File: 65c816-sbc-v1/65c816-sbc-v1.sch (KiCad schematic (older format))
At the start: 50 parts, among them J1 EXPANSION, J2 SIO, J3 VIA_A, J4 VIA_B, J5 power, SW1 RESET, SW2 NMI, U1 W65C816SxP, U10 W65C22SxP, U11 W65C51NxP, U12 74HC138, U15 74HC74, U2 74HC573, U3 74HC245, U4 PAL20L8, U5 PAL20L8, U6 74HC244, U7 74HC244, U8 AS6C4008-55PCN, U9 28C256, X1 28MHz, Y1 1.8432MHz

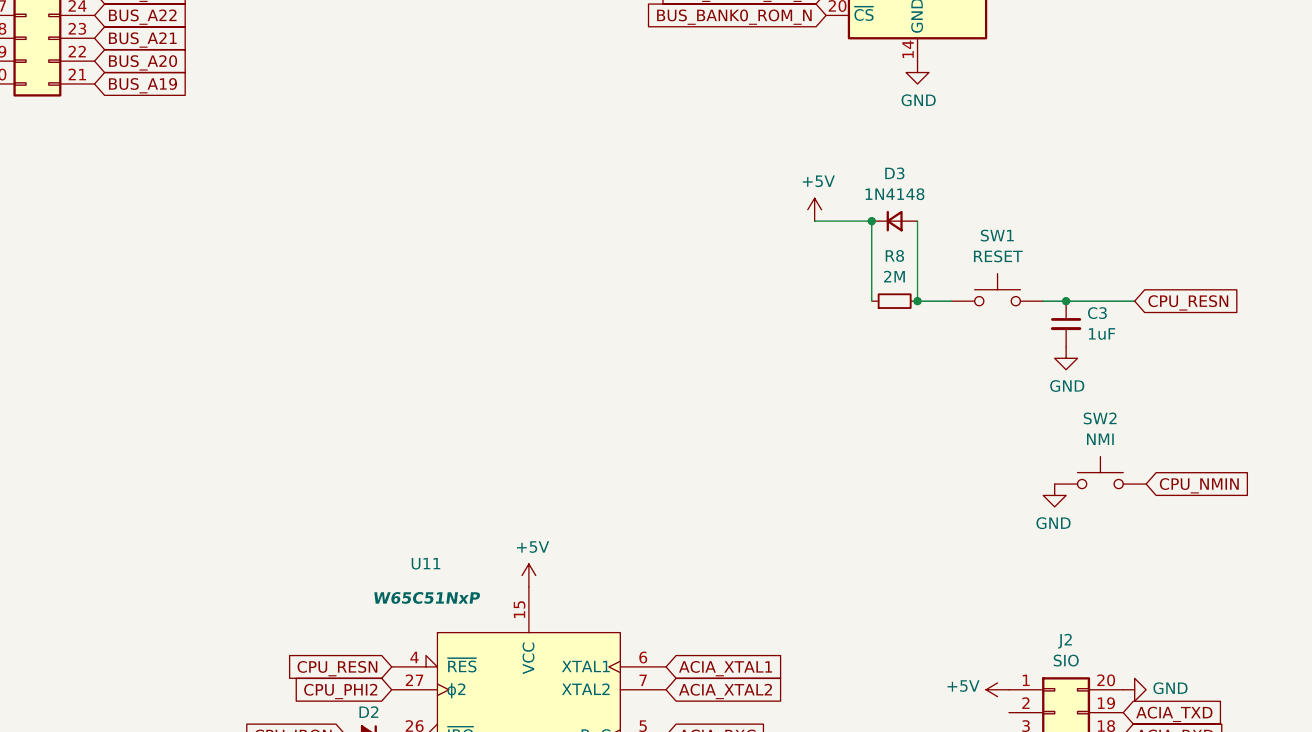
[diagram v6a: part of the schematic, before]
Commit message: Add some LEDs, I may want to wire them up to make sure I'm doing the right thing? Dunno yet.
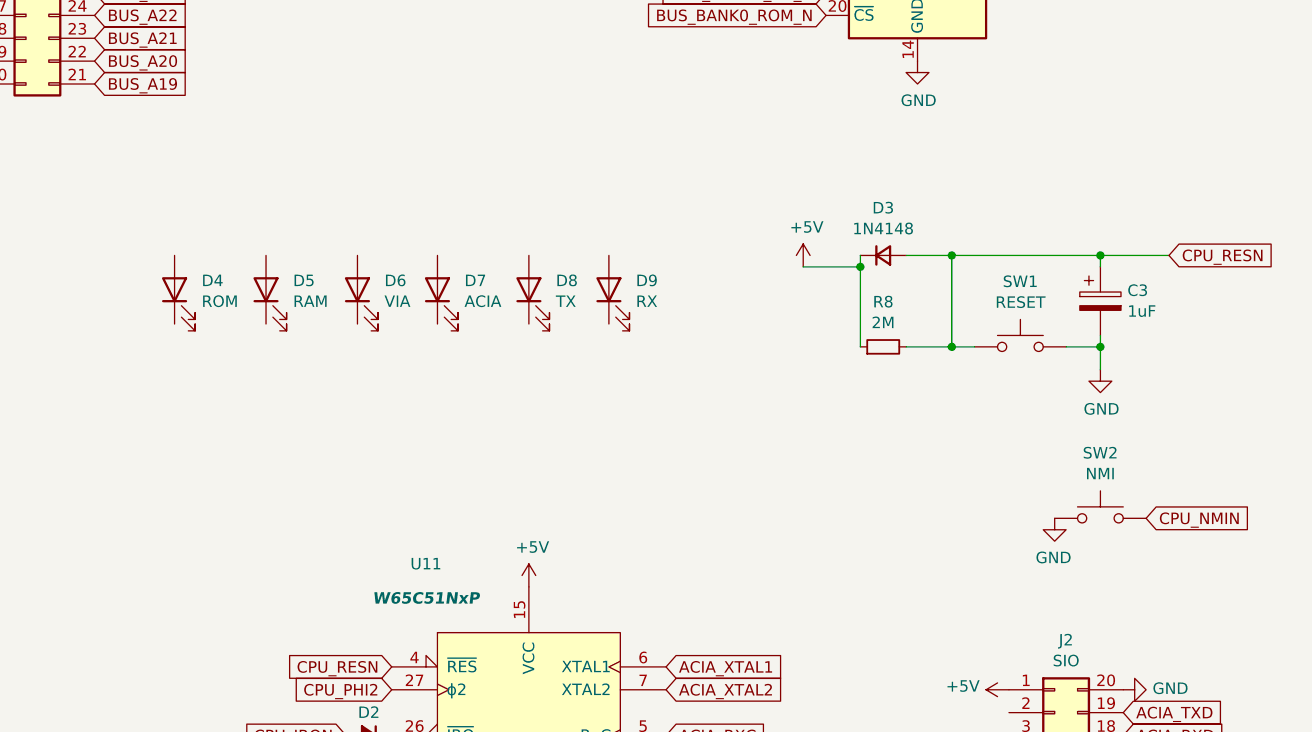
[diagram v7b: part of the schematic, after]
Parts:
- removed C3: 1uF, symbol Device:C_Small
- added C3: 1uF, symbol Device:CP
- added D4: ROM, symbol Device:LED
- added D5: RAM, symbol Device:LED
- added D6: VIA, symbol Device:LED
- added D7: ACIA, symbol Device:LED
- added D8: TX, symbol Device:LED
- added D9: RX, symbol Device:LED
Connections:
- net CPU_RESN: now also D3.2 (A), R8.2, SW1.1, C3.1; no longer SW1.2
- net GND: now also SW1.2, C3.2
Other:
- moved on the sheet: D3, R8, SW1, SW2
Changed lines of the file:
@@
 L Device:D_Small D3
 U 1 1 61DCFAE9
-P 14250 3600
-F 0 "D3" H 14250 3807 50  0000 C CNN
-F 1 "1N4148" H 14250 3716 50  0000 C CNN
-F 2 "Diode_THT:D_DO-35_SOD27_P7.62mm_Horizontal" V 14250 3600 50  0001 C CNN
-F 3 "~" V 14250 3600 50  0001 C CNN
-	1    14250 3600
+P 14200 3750
+F 0 "D3" H 14200 3957 50  0000 C CNN
+F 1 "1N4148" H 14200 3866 50  0000 C CNN
+F 2 "Diode_THT:D_DO-35_SOD27_P7.62mm_Horizontal" V 14200 3750 50  0001 C CNN
+F 3 "~" V 14200 3750 50  0001 C CNN
+	1    14200 3750
 	1    0    0    -1
 $EndComp
@@
 L Device:R_Small R8
 U 1 1 61DD0317
-P 14250 3950
-F 0 "R8" V 14446 3950 50  0000 C CNN
-F 1 "2M" V 14355 3950 50  0000 C CNN
-F 2 "" H 14250 3950 50  0001 C CNN
-F 3 "~" H 14250 3950 50  0001 C CNN
-	1    14250 3950
+P 14200 4150
+F 0 "R8" V 14396 4150 50  0000 C CNN
+F 1 "2M" V 14305 4150 50  0000 C CNN
+F 2 "" H 14200 4150 50  0001 C CNN
+F 3 "~" H 14200 4150 50  0001 C CNN
+	1    14200 4150
 	0    -1   -1   0
-$EndComp
-$Comp
-L Device:C_Small C3
-U 1 1 61DD0F01
-P 15000 4050
-F 0 "C3" H 15092 4096 50  0000 L CNN
-F 1 "1uF" H 15092 4005 50  0000 L CNN
-F 2 "" H 15000 4050 50  0001 C CNN
-F 3 "~" H 15000 4050 50  0001 C CNN
-	1    15000 4050
-	1    0    0    -1
 $EndComp
 $Comp
 L Switch:SW_Push SW1
 U 1 1 61DD2E7B
-P 14700 3950
-F 0 "SW1" H 14700 4235 50  0000 C CNN
-F 1 "RESET" H 14700 4144 50  0000 C CNN
-F 2 "" H 14700 4150 50  0001 C CNN
-F 3 "~" H 14700 4150 50  0001 C CNN
-	1    14700 3950
+P 14800 4150
+F 0 "SW1" H 14800 4435 50  0000 C CNN
+F 1 "RESET" H 14800 4344 50  0000 C CNN
+F 2 "" H 14800 4350 50  0001 C CNN
+F 3 "~" H 14800 4350 50  0001 C CNN
+	1    14800 4150
 	1    0    0    -1
 $EndComp
@@
 L Switch:SW_Push SW2
 U 1 1 61DD3596
-P 15150 4750
-F 0 "SW2" H 15150 5035 50  0000 C CNN
-F 1 "NMI" H 15150 4944 50  0000 C CNN
-F 2 "" H 15150 4950 50  0001 C CNN
-F 3 "~" H 15150 4950 50  0001 C CNN
-	1    15150 4750
+P 15150 4900
+F 0 "SW2" H 15150 5185 50  0000 C CNN
+F 1 "NMI" H 15150 5094 50  0000 C CNN
+F 2 "" H 15150 5100 50  0001 C CNN
+F 3 "~" H 15150 5100 50  0001 C CNN
+	1    15150 4900
 	-1   0    0    -1
 $EndComp
@@
 L power:GND #PWR0141
 U 1 1 61D6FDD3
-P 14950 4750
-F 0 "#PWR0141" H 14950 4500 50  0001 C CNN
-F 1 "GND" H 14955 4577 50  0000 C CNN
-F 2 "" H 14950 4750 50  0001 C CNN
-F 3 "" H 14950 4750 50  0001 C CNN
-	1    14950 4750
+P 14950 4900
+F 0 "#PWR0141" H 14950 4650 50  0001 C CNN
+F 1 "GND" H 14955 4727 50  0000 C CNN
+F 2 "" H 14950 4900 50  0001 C CNN
+F 3 "" H 14950 4900 50  0001 C CNN
+	1    14950 4900
 	-1   0    0    -1
 $EndComp
-Text GLabel 15350 4750 2    50   Input ~ 0
+Text GLabel 15350 4900 2    50   Input ~ 0
 CPU_NMIN
 Wire Wire Line
-	14150 3600 14150 3950
-Wire Wire Line
-	14350 3600 14350 3950
+	14100 3800 14100 4150
 $Comp
 L power:+5V #PWR0142
 U 1 1 61D85F0E
-P 13900 3600
-F 0 "#PWR0142" H 13900 3450 50  0001 C CNN
-F 1 "+5V" H 13915 3773 50  0000 C CNN
-F 2 "" H 13900 3600 50  0001 C CNN
-F 3 "" H 13900 3600 50  0001 C CNN
-	1    13900 3600
-	1    0    0    -1
-$EndComp
-Wire Wire Line
-	13900 3600 14150 3600
-Connection ~ 14150 3600
-Wire Wire Line
-	15000 3950 14900 3950
-Wire Wire Line
-	14500 3950 14350 3950
-Connection ~ 14350 3950
+P 13850 3800
+F 0 "#PWR0142" H 13850 3650 50  0001 C CNN
+F 1 "+5V" H 13865 3973 50  0000 C CNN
+F 2 "" H 13850 3800 50  0001 C CNN
+F 3 "" H 13850 3800 50  0001 C CNN
+	1    13850 3800
+	1    0    0    -1
+$EndComp
+Wire Wire Line
+	13850 3800 14100 3800
 $Comp
 L power:GND #PWR0143
 U 1 1 61D967F7
-P 15000 4150
-F 0 "#PWR0143" H 15000 3900 50  0001 C CNN
-F 1 "GND" H 15005 3977 50  0000 C CNN
-F 2 "" H 15000 4150 50  0001 C CNN
-F 3 "" H 15000 4150 50  0001 C CNN
-	1    15000 4150
-	1    0    0    -1
-$EndComp
-Text GLabel 15300 3950 2    50   Input ~ 0
+P 15150 4250
+F 0 "#PWR0143" H 15150 4000 50  0001 C CNN
+F 1 "GND" H 15155 4077 50  0000 C CNN
+F 2 "" H 15150 4250 50  0001 C CNN
+F 3 "" H 15150 4250 50  0001 C CNN
+	1    15150 4250
+	1    0    0    -1
+$EndComp
+Text GLabel 15450 3750 2    50   Input ~ 0
 CPU_RESN
-Wire Wire Line
-	15300 3950 15000 3950
-Connection ~ 15000 3950
 $Comp
 L Device:C_Small C32
@@
 	1    0    0    -1
 $EndComp
+Wire Wire Line
+	14300 4150 14500 4150
+Wire Wire Line
+	14100 3750 14100 3800
+Connection ~ 14100 3800
+Wire Wire Line
+	14300 3750 14500 3750
+Wire Wire Line
+	14500 3750 14500 4150
+Connection ~ 14500 3750
+Connection ~ 14500 4150
+Wire Wire Line
+	14600 4150 14500 4150
+Wire Wire Line
+	15000 4150 15150 4150
+Wire Wire Line
+	15150 4150 15150 4250
+$Comp
+L Device:CP C3
+U 1 1 61ECEEFB
+P 15150 3950
+F 0 "C3" H 15268 3996 50  0000 L CNN
+F 1 "1uF" H 15268 3905 50  0000 L CNN
+F 2 "" H 15188 3800 50  0001 C CNN
+F 3 "~" H 15150 3950 50  0001 C CNN
+	1    15150 3950
+	1    0    0    -1
+$EndComp
+Wire Wire Line
+	14500 3750 15150 3750
+Wire Wire Line
+	15150 3800 15150 3750
+Connection ~ 15150 3750
+Wire Wire Line
+	15150 3750 15450 3750
+Wire Wire Line
+	15150 4100 15150 4150
+Connection ~ 15150 4150
+$Comp
+L Device:LED D4
+U 1 1 61EE19AC
+P 11100 3900
+F 0 "D4" V 11139 3782 50  0000 R CNN
+F 1 "ROM" V 11048 3782 50  0000 R CNN
+F 2 "" H 11100 3900 50  0001 C CNN
+F 3 "~" H 11100 3900 50  0001 C CNN
+	1    11100 3900
+	0    -1   -1   0
+$EndComp
+$Comp
+L Device:LED D5
+U 1 1 61EEF02B
+P 11500 3900
+F 0 "D5" V 11539 3782 50  0000 R CNN
+F 1 "RAM" V 11448 3782 50  0000 R CNN
+F 2 "" H 11500 3900 50  0001 C CNN
+F 3 "~" H 11500 3900 50  0001 C CNN
+	1    11500 3900
+	0    -1   -1   0
+$EndComp
+$Comp
+L Device:LED D6
+U 1 1 61EF1D84
+P 11900 3900
+F 0 "D6" V 11939 3782 50  0000 R CNN
+F 1 "VIA" V 11848 3782 50  0000 R CNN
+F 2 "" H 11900 3900 50  0001 C CNN
+F 3 "~" H 11900 3900 50  0001 C CNN
+	1    11900 3900
+	0    -1   -1   0
+$EndComp
+$Comp
+L Device:LED D7
+U 1 1 61EF8861
+P 12250 3900
+F 0 "D7" V 12289 3782 50  0000 R CNN
+F 1 "ACIA" V 12198 3782 50  0000 R CNN
+F 2 "" H 12250 3900 50  0001 C CNN
+F 3 "~" H 12250 3900 50  0001 C CNN
+	1    12250 3900
+	0    -1   -1   0
+$EndComp
+$Comp
+L Device:LED D8
+U 1 1 61EFD25B
+P 12650 3900
+F 0 "D8" V 12689 3782 50  0000 R CNN
+F 1 "TX" V 12598 3782 50  0000 R CNN
+F 2 "" H 12650 3900 50  0001 C CNN
+F 3 "~" H 12650 3900 50  0001 C CNN
+	1    12650 3900
+	0    -1   -1   0
+$EndComp
+$Comp
+L Device:LED D9
+U 1 1 61F004E4
+P 13000 3900
+F 0 "D9" V 13039 3782 50  0000 R CNN
+F 1 "RX" V 12948 3782 50  0000 R CNN
+F 2 "" H 13000 3900 50  0001 C CNN
+F 3 "~" H 13000 3900 50  0001 C CNN
+	1    13000 3900
+	0    -1   -1   0
+$EndComp
 $EndSCHEMATC

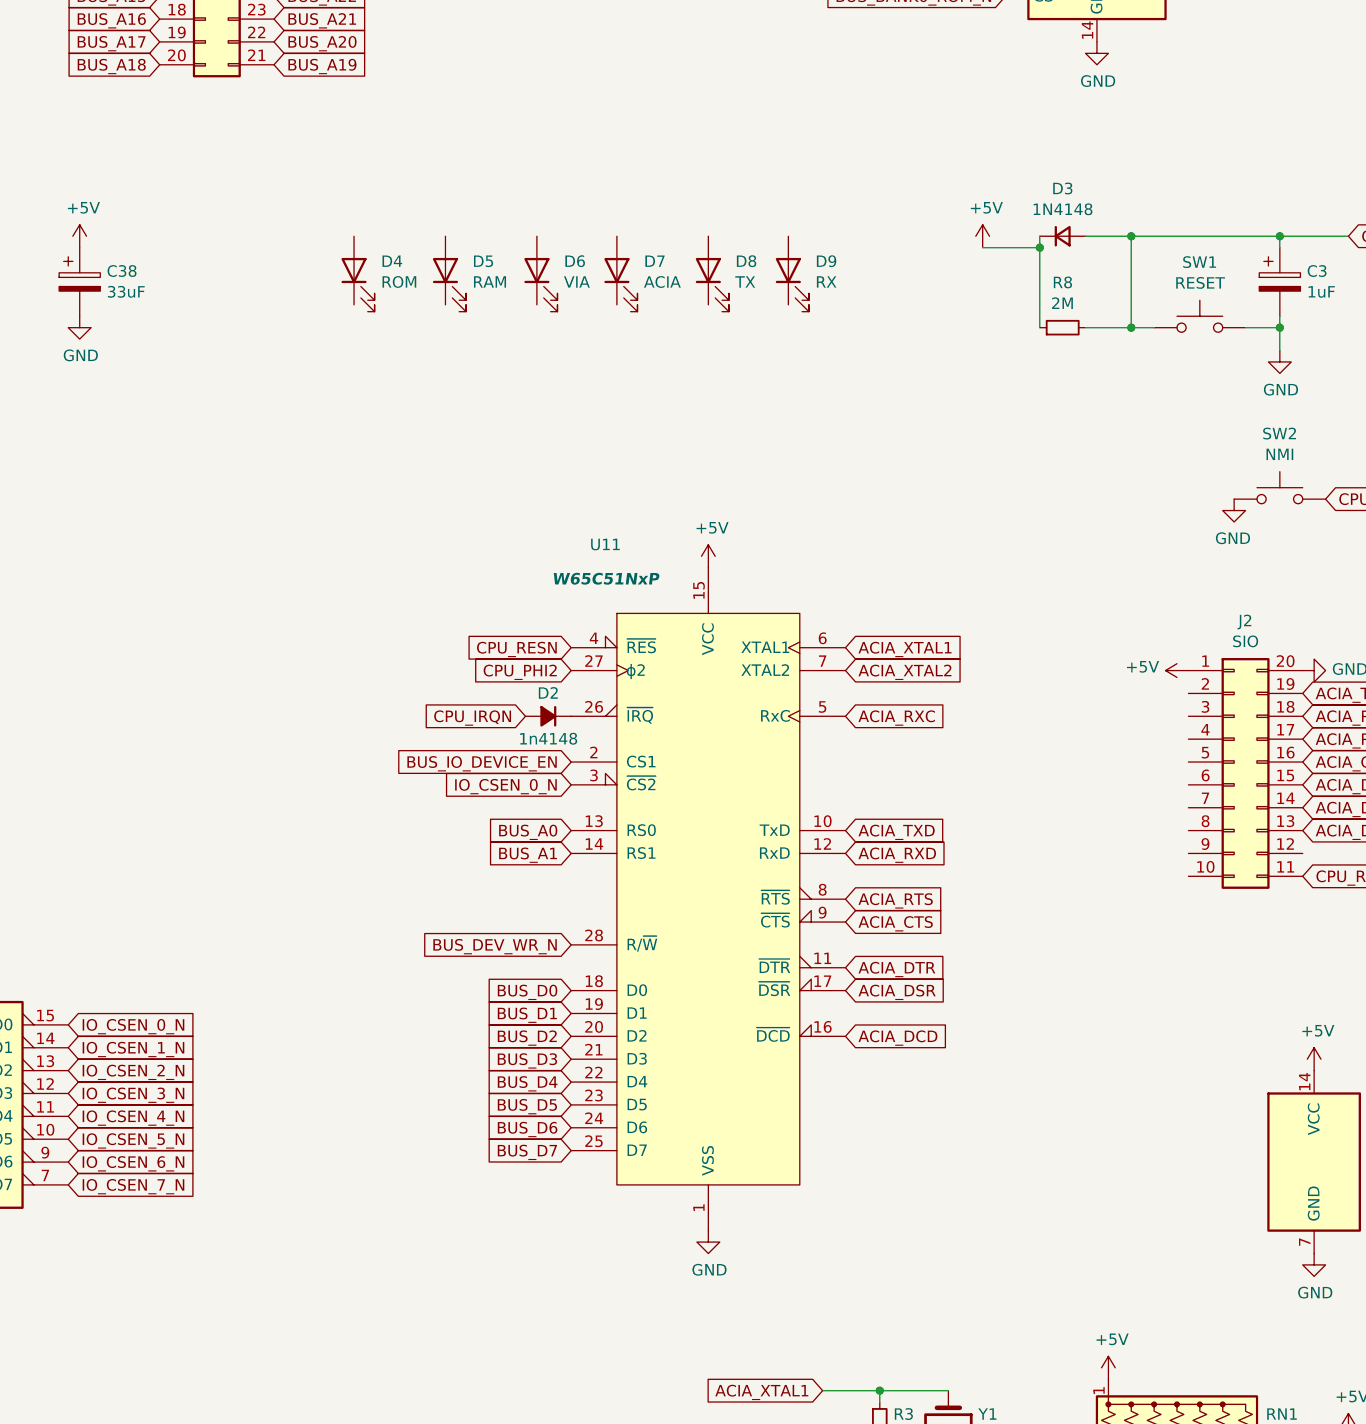
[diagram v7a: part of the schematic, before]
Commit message: updates; started routing it
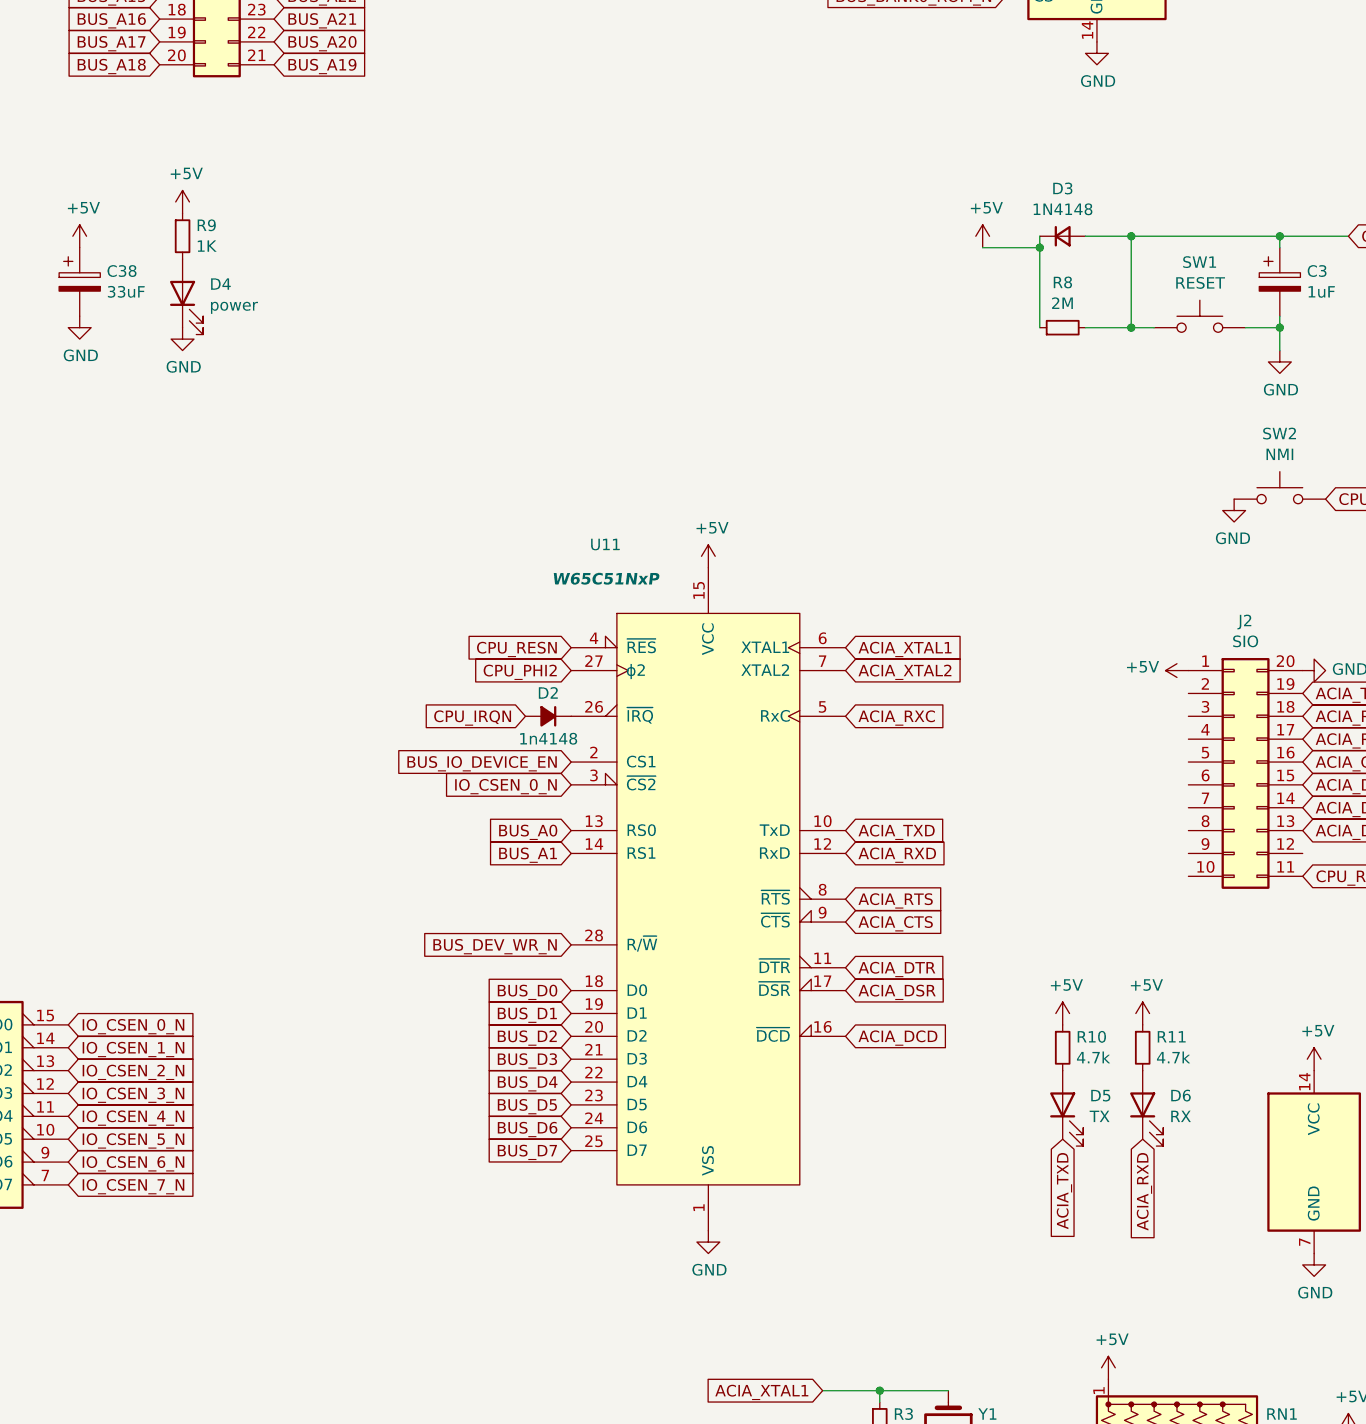
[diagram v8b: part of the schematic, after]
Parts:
- removed D5: RAM, symbol Device:LED
- removed D6: VIA, symbol Device:LED
- removed D7: ACIA, symbol Device:LED
- added R10, R11: 4.7k, Resistor_THT:R_Axial_DIN0207_L6.3mm_D2.5mm_P5.08mm_Vertical, symbol Device:R_Small
- added R9: 1K, Resistor_THT:R_Axial_DIN0207_L6.3mm_D2.5mm_P5.08mm_Vertical, symbol Device:R_Small
- C1, C20, C21, C22, C23, C24, C25, C26, C27, C28, C29, C30, C31, C32, C33, C34, C35, C36, C37: footprint (none) -> Capacitor_THT:C_Rect_L7.5mm_W6.5mm_P5.00mm
- C3, C38: footprint (none) -> Capacitor_THT:CP_Radial_D10.0mm_P7.50mm
- D4: value ROM -> power; footprint (none) -> LED_THT:LED_D4.0mm
- D5: renamed from D8; footprint (none) -> LED_THT:LED_D4.0mm
- D6: renamed from D9; footprint (none) -> LED_THT:LED_D4.0mm
- J5: footprint (none) -> Connector_PinHeader_2.54mm:PinHeader_1x02_P2.54mm_Vertical
- R2, R3, R8: footprint (none) -> Resistor_THT:R_Axial_DIN0207_L6.3mm_D2.5mm_P5.08mm_Vertical
- SW1, SW2: footprint (none) -> Button_Switch_THT:KSA_Tactile_SPST
- U1, U10, U11: footprint Package_DIP:DIP-40_W25.4mm_Socket -> Package_DIP:DIP-40_W15.24mm_Socket
- U4, U5: footprint Package_DIP:DIP-24_W15.24mm_Socket -> Package_DIP:DIP-24_W7.62mm_Socket
- U9: footprint Package_DIP:DIP-28_W7.62mm_Socket -> Package_DIP:DIP-28_W15.24mm_Socket
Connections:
- net +5V: now also R10.1, R11.1, R9.1
- net ACIA_RXD: now also D6.1 (K)
- net ACIA_TXD: now also D5.1 (K)
- net GND: now also D4.1 (K)
- net at D4.2 (A): now also R9.2
- net at D5.2 (A): now also R10.2
- net at D6.2 (A): now also R11.2
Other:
- moved on the sheet: D5, D6
